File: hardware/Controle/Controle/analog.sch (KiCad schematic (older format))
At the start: 19 parts

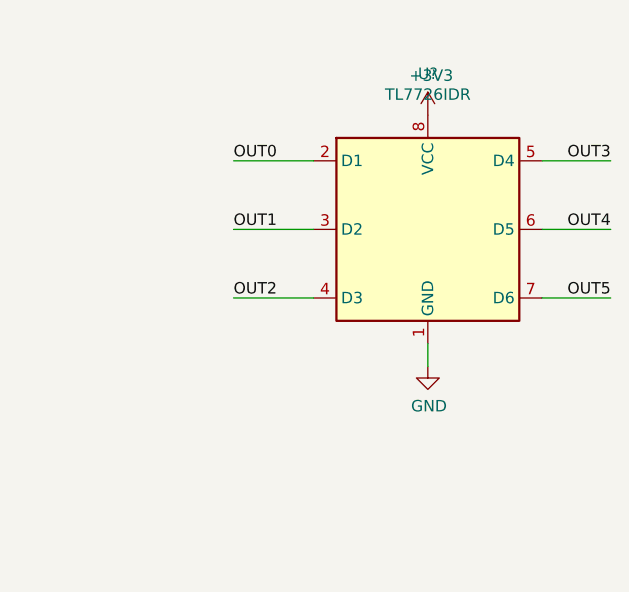
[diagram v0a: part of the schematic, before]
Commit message: adicionado o TL7726 e modificada a placa
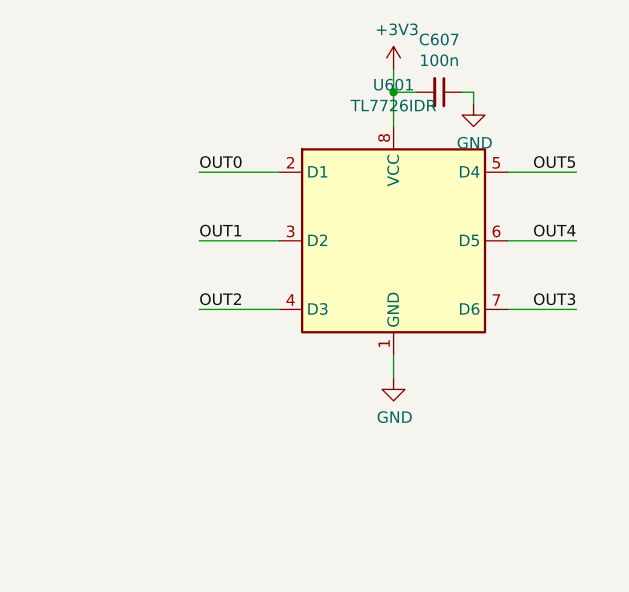
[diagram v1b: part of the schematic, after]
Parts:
- added C607: 100n, Capacitor_SMD:C_0603_1608Metric_Pad1.08x0.95mm_HandSolder, symbol Device:C_Small
- U601: renamed from U?; footprint Package_SON:X2SON-8_1.4x1mm_P0.35mm -> Package_SO:SOIC-8_3.9x4.9mm_P1.27mm
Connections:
- net +3V3: now also C607.2
- net GND: now also C607.1
- net Out3: now also U601.7 (D6); no longer U601.5 (D4)
- net Out5: now also U601.5 (D4); no longer U601.7 (D6)
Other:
- moved on the sheet: U601
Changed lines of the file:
@@
 In0
 $Comp
-L tl7726:TL7726IDR U?
+L tl7726:TL7726IDR U601
 U 1 1 60A10993
-P 5000 1400
-F 0 "U?" H 5000 2081 50  0000 C CNN
-F 1 "TL7726IDR" H 5000 1990 50  0000 C CNN
-F 2 "Package_SON:X2SON-8_1.4x1mm_P0.35mm" H 4050 900 50  0001 C CNN
-F 3 "http://www.ti.com/lit/ds/symlink/tpd4s1394.pdf" H 4900 1350 50  0001 C CNN
-	1    5000 1400
+P 4850 1450
+F 0 "U601" H 4850 2131 50  0000 C CNN
+F 1 "TL7726IDR" H 4850 2040 50  0000 C CNN
+F 2 "Package_SO:SOIC-8_3.9x4.9mm_P1.27mm" H 3900 950 50  0001 C CNN
+F 3 "http://www.ti.com/lit/ds/symlink/tpd4s1394.pdf" H 4750 1400 50  0001 C CNN
+	1    4850 1450
 	1    0    0    -1
 $EndComp
@@
 Text Label 2350 4350 0    50   ~ 0
 OUT5
-Text Label 4150 1100 0    50   ~ 0
+Text Label 4000 1150 0    50   ~ 0
 OUT0
 Wire Wire Line
-	4150 1100 4500 1100
-Text Label 4150 1400 0    50   ~ 0
+	4000 1150 4350 1150
+Text Label 4000 1450 0    50   ~ 0
 OUT1
 Wire Wire Line
-	4150 1400 4500 1400
-Text Label 4150 1700 0    50   ~ 0
+	4000 1450 4350 1450
+Text Label 4000 1750 0    50   ~ 0
 OUT2
 Wire Wire Line
-	4150 1700 4500 1700
-Text Label 5800 1100 2    50   ~ 0
+	4000 1750 4350 1750
+Text Label 5650 1750 2    50   ~ 0
 OUT3
 Wire Wire Line
-	5800 1100 5500 1100
-Text Label 5800 1400 2    50   ~ 0
+	5650 1150 5350 1150
+Text Label 5650 1450 2    50   ~ 0
 OUT4
 Wire Wire Line
-	5800 1400 5500 1400
-Text Label 5800 1700 2    50   ~ 0
+	5650 1450 5350 1450
+Text Label 5650 1150 2    50   ~ 0
 OUT5
 Wire Wire Line
-	5800 1700 5500 1700
+	5650 1750 5350 1750
 $Comp
-L power:GND #PWR?
+L power:GND #PWR0119
 U 1 1 60A2814F
-P 5000 2000
-F 0 "#PWR?" H 5000 1750 50  0001 C CNN
-F 1 "GND" H 5005 1827 50  0000 C CNN
-F 2 "" H 5000 2000 50  0001 C CNN
-F 3 "" H 5000 2000 50  0001 C CNN
-	1    5000 2000
+P 4850 2050
+F 0 "#PWR0119" H 4850 1800 50  0001 C CNN
+F 1 "GND" H 4855 1877 50  0000 C CNN
+F 2 "" H 4850 2050 50  0001 C CNN
+F 3 "" H 4850 2050 50  0001 C CNN
+	1    4850 2050
 	1    0    0    -1
 $EndComp
 Wire Wire Line
-	5000 2000 5000 1900
+	4850 2050 4850 1950
 $Comp
-L power:+3V3 #PWR?
+L power:+3V3 #PWR0120
 U 1 1 60A2A838
 P 1000 2350
-F 0 "#PWR?" H 1000 2200 50  0001 C CNN
+F 0 "#PWR0120" H 1000 2200 50  0001 C CNN
 F 1 "+3V3" H 1015 2523 50  0000 C CNN
 F 2 "" H 1000 2350 50  0001 C CNN
@@
 	1000 2550 1000 2350
 $Comp
-L power:+3V3 #PWR?
+L power:+3V3 #PWR0121
 U 1 1 60A2DB9D
-P 5000 900
-F 0 "#PWR?" H 5000 750 50  0001 C CNN
-F 1 "+3V3" H 5015 1073 50  0000 C CNN
-F 2 "" H 5000 900 50  0001 C CNN
-F 3 "" H 5000 900 50  0001 C CNN
-	1    5000 900
+P 4850 700
+F 0 "#PWR0121" H 4850 550 50  0001 C CNN
+F 1 "+3V3" H 4865 873 50  0000 C CNN
+F 2 "" H 4850 700 50  0001 C CNN
+F 3 "" H 4850 700 50  0001 C CNN
+	1    4850 700
 	1    0    0    -1
 $EndComp
@@
 Wire Wire Line
 	2100 4350 2600 4350
+$Comp
+L Device:C_Small C607
+U 1 1 60A6394D
+P 5050 800
+F 0 "C607" V 4821 800 50  0000 C CNN
+F 1 "100n" V 4912 800 50  0000 C CNN
+F 2 "Capacitor_SMD:C_0603_1608Metric_Pad1.08x0.95mm_HandSolder" H 5050 800 50  0001 C CNN
+F 3 "~" H 5050 800 50  0001 C CNN
+	1    5050 800
+	0    1    1    0
+$EndComp
+Wire Wire Line
+	4850 700  4850 800
+$Comp
+L power:GND #PWR0122
+U 1 1 60A69EE4
+P 5200 850
+F 0 "#PWR0122" H 5200 600 50  0001 C CNN
+F 1 "GND" H 5205 677 50  0000 C CNN
+F 2 "" H 5200 850 50  0001 C CNN
+F 3 "" H 5200 850 50  0001 C CNN
+	1    5200 850
+	1    0    0    -1
+$EndComp
+Wire Wire Line
+	5200 850  5200 800
+Wire Wire Line
+	5200 800  5150 800
+Wire Wire Line
+	4950 800  4850 800
+Connection ~ 4850 800
+Wire Wire Line
+	4850 800  4850 950
 $EndSCHEMATC

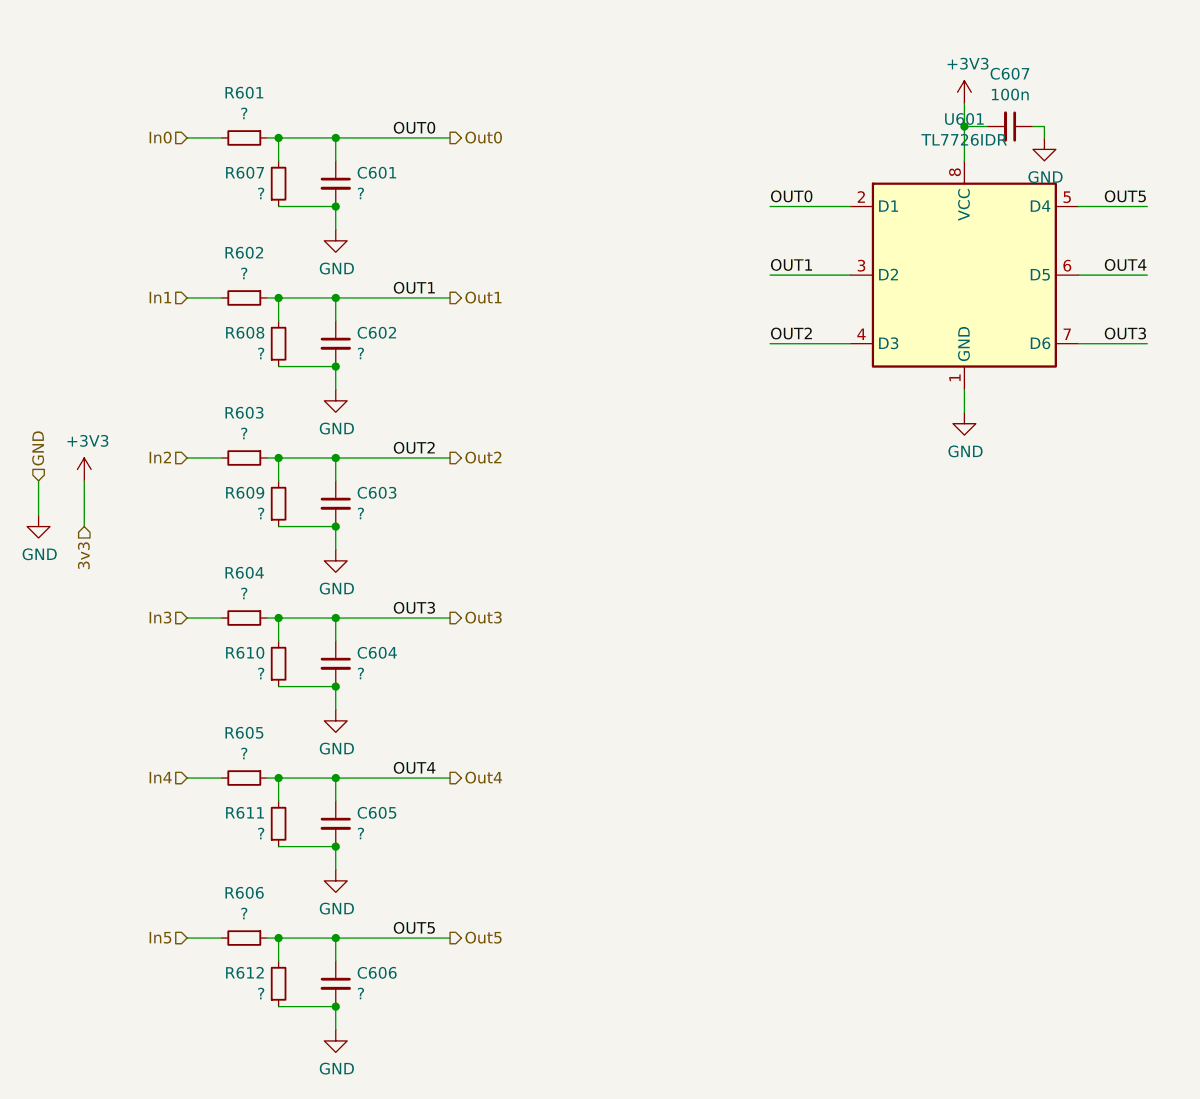
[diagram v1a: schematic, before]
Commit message: control PCB updated
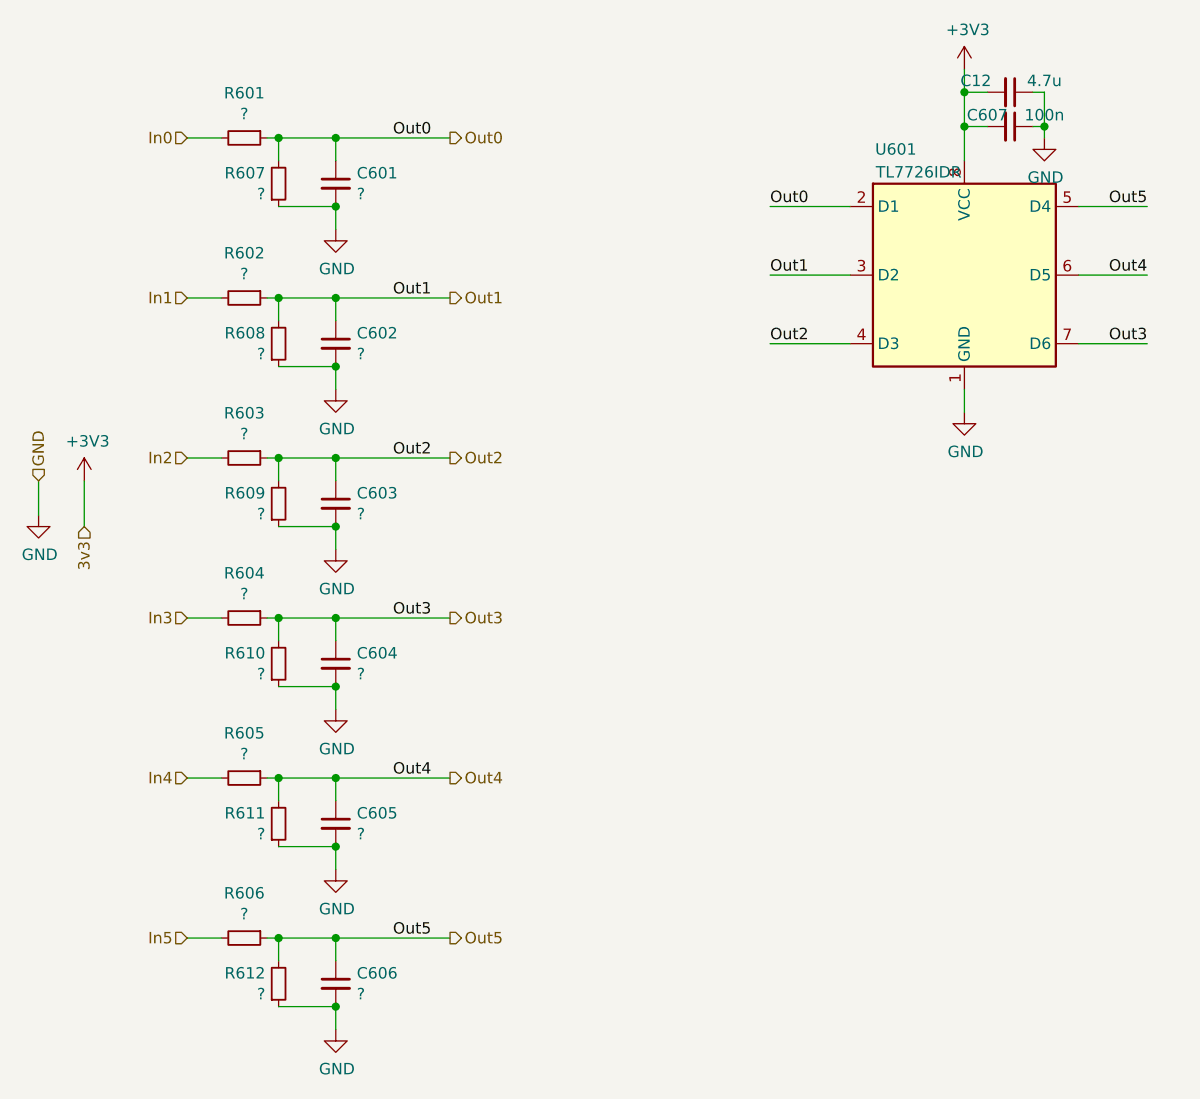
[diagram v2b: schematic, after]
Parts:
- added C12: 4.7u, Capacitor_SMD:C_1210_3225Metric_Pad1.33x2.70mm_HandSolder, symbol Device:C_Small
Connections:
- net +3V3: now also C12.2
- net GND: now also C12.1
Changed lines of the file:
@@
 U 1 1 60A10993
 P 4850 1450
-F 0 "U601" H 4850 2131 50  0000 C CNN
-F 1 "TL7726IDR" H 4850 2040 50  0000 C CNN
+F 0 "U601" H 4550 2000 50  0000 C CNN
+F 1 "TL7726IDR" H 4650 1900 50  0000 C CNN
 F 2 "Package_SO:SOIC-8_3.9x4.9mm_P1.27mm" H 3900 950 50  0001 C CNN
 F 3 "http://www.ti.com/lit/ds/symlink/tpd4s1394.pdf" H 4750 1400 50  0001 C CNN
@@
 $EndComp
 Text Label 2350 850  0    50   ~ 0
-OUT0
+Out0
 Text Label 2350 1550 0    50   ~ 0
-OUT1
+Out1
 Text Label 2350 2250 0    50   ~ 0
-OUT2
+Out2
 Text Label 2350 2950 0    50   ~ 0
-OUT3
+Out3
 Text Label 2350 3650 0    50   ~ 0
-OUT4
+Out4
 Text Label 2350 4350 0    50   ~ 0
-OUT5
+Out5
 Text Label 4000 1150 0    50   ~ 0
-OUT0
+Out0
 Wire Wire Line
 	4000 1150 4350 1150
 Text Label 4000 1450 0    50   ~ 0
-OUT1
+Out1
 Wire Wire Line
 	4000 1450 4350 1450
 Text Label 4000 1750 0    50   ~ 0
-OUT2
+Out2
 Wire Wire Line
 	4000 1750 4350 1750
 Text Label 5650 1750 2    50   ~ 0
-OUT3
+Out3
 Wire Wire Line
 	5650 1150 5350 1150
 Text Label 5650 1450 2    50   ~ 0
-OUT4
+Out4
 Wire Wire Line
 	5650 1450 5350 1450
 Text Label 5650 1150 2    50   ~ 0
-OUT5
+Out5
 Wire Wire Line
 	5650 1750 5350 1750
@@
 L power:+3V3 #PWR0121
 U 1 1 60A2DB9D
-P 4850 700
-F 0 "#PWR0121" H 4850 550 50  0001 C CNN
-F 1 "+3V3" H 4865 873 50  0000 C CNN
-F 2 "" H 4850 700 50  0001 C CNN
-F 3 "" H 4850 700 50  0001 C CNN
-	1    4850 700
+P 4850 550
+F 0 "#PWR0121" H 4850 400 50  0001 C CNN
+F 1 "+3V3" H 4865 723 50  0000 C CNN
+F 2 "" H 4850 550 50  0001 C CNN
+F 3 "" H 4850 550 50  0001 C CNN
+	1    4850 550
 	1    0    0    -1
 $EndComp
@@
 U 1 1 60A6394D
 P 5050 800
-F 0 "C607" V 4821 800 50  0000 C CNN
-F 1 "100n" V 4912 800 50  0000 C CNN
+F 0 "C607" V 5000 700 50  0000 C CNN
+F 1 "100n" V 5000 950 50  0000 C CNN
 F 2 "Capacitor_SMD:C_0603_1608Metric_Pad1.08x0.95mm_HandSolder" H 5050 800 50  0001 C CNN
 F 3 "~" H 5050 800 50  0001 C CNN
@@
 $EndComp
 Wire Wire Line
-	4850 700  4850 800
+	4850 550  4850 650
 $Comp
 L power:GND #PWR0122
@@
 Wire Wire Line
 	4850 800  4850 950
+$Comp
+L Device:C_Small C12
+U 1 1 607A1571
+P 5050 650
+F 0 "C12" V 5000 500 50  0000 C CNN
+F 1 "4.7u" V 5000 800 50  0000 C CNN
+F 2 "Capacitor_SMD:C_1210_3225Metric_Pad1.33x2.70mm_HandSolder" H 5050 650 50  0001 C CNN
+F 3 "~" H 5050 650 50  0001 C CNN
+	1    5050 650
+	0    1    1    0
+$EndComp
+Wire Wire Line
+	5150 650  5200 650
+Wire Wire Line
+	5200 650  5200 800
+Connection ~ 5200 800
+Wire Wire Line
+	4950 650  4850 650
+Connection ~ 4850 650
+Wire Wire Line
+	4850 650  4850 800
 $EndSCHEMATC

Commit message: falta acabamento
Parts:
- C12: footprint Capacitor_SMD:C_1210_3225Metric_Pad1.33x2.70mm_HandSolder -> Capacitor_SMD:C_1206_3216Metric_Pad1.33x1.80mm_HandSolder
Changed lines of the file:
@@
 F 0 "C12" V 5000 500 50  0000 C CNN
 F 1 "4.7u" V 5000 800 50  0000 C CNN
-F 2 "Capacitor_SMD:C_1210_3225Metric_Pad1.33x2.70mm_HandSolder" H 5050 650 50  0001 C CNN
+F 2 "Capacitor_SMD:C_1206_3216Metric_Pad1.33x1.80mm_HandSolder" H 5050 650 50  0001 C CNN
 F 3 "~" H 5050 650 50  0001 C CNN
 	1    5050 650

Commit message: vias
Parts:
- C601, C602, C603: value ? -> 1n
- C604: value ? -> 100n
- R601, R602, R603: value ? -> 10k
- R604: value ? -> 0R
- R605, R606, R610, R611, R612: value ? -> NC
- R607, R608, R609: value ? -> 3k3
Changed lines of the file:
@@
 P 1700 1550
 F 0 "R602" V 1504 1550 50  0000 C CNN
-F 1 "?" V 1595 1550 50  0000 C CNN
+F 1 "10k" V 1595 1550 50  0000 C CNN
 F 2 "Resistor_SMD:R_0603_1608Metric_Pad0.98x0.95mm_HandSolder" H 1700 1550 50  0001 C CNN
 F 3 "~" H 1700 1550 50  0001 C CNN
@@
 P 2100 1750
 F 0 "C602" H 2192 1796 50  0000 L CNN
-F 1 "?" H 2192 1705 50  0000 L CNN
+F 1 "1n" H 2192 1705 50  0000 L CNN
 F 2 "Capacitor_SMD:C_0603_1608Metric_Pad1.08x0.95mm_HandSolder" H 2100 1750 50  0001 C CNN
 F 3 "~" H 2100 1750 50  0001 C CNN
@@
 P 1850 1750
 F 0 "R608" H 1792 1704 50  0000 R CNN
-F 1 "?" H 1792 1795 50  0000 R CNN
+F 1 "3k3" H 1792 1795 50  0000 R CNN
 F 2 "Resistor_SMD:R_0603_1608Metric_Pad0.98x0.95mm_HandSolder" H 1850 1750 50  0001 C CNN
 F 3 "~" H 1850 1750 50  0001 C CNN
@@
 P 1700 2250
 F 0 "R603" V 1504 2250 50  0000 C CNN
-F 1 "?" V 1595 2250 50  0000 C CNN
+F 1 "10k" V 1595 2250 50  0000 C CNN
 F 2 "Resistor_SMD:R_0603_1608Metric_Pad0.98x0.95mm_HandSolder" H 1700 2250 50  0001 C CNN
 F 3 "~" H 1700 2250 50  0001 C CNN
@@
 P 2100 2450
 F 0 "C603" H 2192 2496 50  0000 L CNN
-F 1 "?" H 2192 2405 50  0000 L CNN
+F 1 "1n" H 2192 2405 50  0000 L CNN
 F 2 "Capacitor_SMD:C_0603_1608Metric_Pad1.08x0.95mm_HandSolder" H 2100 2450 50  0001 C CNN
 F 3 "~" H 2100 2450 50  0001 C CNN
@@
 P 1850 2450
 F 0 "R609" H 1792 2404 50  0000 R CNN
-F 1 "?" H 1792 2495 50  0000 R CNN
+F 1 "3k3" H 1792 2495 50  0000 R CNN
 F 2 "Resistor_SMD:R_0603_1608Metric_Pad0.98x0.95mm_HandSolder" H 1850 2450 50  0001 C CNN
 F 3 "~" H 1850 2450 50  0001 C CNN
@@
 P 1700 2950
 F 0 "R604" V 1504 2950 50  0000 C CNN
-F 1 "?" V 1595 2950 50  0000 C CNN
+F 1 "0R" V 1595 2950 50  0000 C CNN
 F 2 "Resistor_SMD:R_0603_1608Metric_Pad0.98x0.95mm_HandSolder" H 1700 2950 50  0001 C CNN
 F 3 "~" H 1700 2950 50  0001 C CNN
@@
 P 2100 3150
 F 0 "C604" H 2192 3196 50  0000 L CNN
-F 1 "?" H 2192 3105 50  0000 L CNN
+F 1 "100n" H 2192 3105 50  0000 L CNN
 F 2 "Capacitor_SMD:C_0603_1608Metric_Pad1.08x0.95mm_HandSolder" H 2100 3150 50  0001 C CNN
 F 3 "~" H 2100 3150 50  0001 C CNN
@@
 P 1850 3150
 F 0 "R610" H 1792 3104 50  0000 R CNN
-F 1 "?" H 1792 3195 50  0000 R CNN
+F 1 "NC" H 1792 3195 50  0000 R CNN
 F 2 "Resistor_SMD:R_0603_1608Metric_Pad0.98x0.95mm_HandSolder" H 1850 3150 50  0001 C CNN
 F 3 "~" H 1850 3150 50  0001 C CNN
@@
 P 1700 3650
 F 0 "R605" V 1504 3650 50  0000 C CNN
-F 1 "?" V 1595 3650 50  0000 C CNN
+F 1 "NC" V 1595 3650 50  0000 C CNN
 F 2 "Resistor_SMD:R_0603_1608Metric_Pad0.98x0.95mm_HandSolder" H 1700 3650 50  0001 C CNN
 F 3 "~" H 1700 3650 50  0001 C CNN
@@
 P 1850 3850
 F 0 "R611" H 1792 3804 50  0000 R CNN
-F 1 "?" H 1792 3895 50  0000 R CNN
+F 1 "NC" H 1792 3895 50  0000 R CNN
 F 2 "Resistor_SMD:R_0603_1608Metric_Pad0.98x0.95mm_HandSolder" H 1850 3850 50  0001 C CNN
 F 3 "~" H 1850 3850 50  0001 C CNN
@@
 P 1700 4350
 F 0 "R606" V 1504 4350 50  0000 C CNN
-F 1 "?" V 1595 4350 50  0000 C CNN
+F 1 "NC" V 1595 4350 50  0000 C CNN
 F 2 "Resistor_SMD:R_0603_1608Metric_Pad0.98x0.95mm_HandSolder" H 1700 4350 50  0001 C CNN
 F 3 "~" H 1700 4350 50  0001 C CNN
@@
 P 1850 4550
 F 0 "R612" H 1792 4504 50  0000 R CNN
-F 1 "?" H 1792 4595 50  0000 R CNN
+F 1 "NC" H 1792 4595 50  0000 R CNN
 F 2 "Resistor_SMD:R_0603_1608Metric_Pad0.98x0.95mm_HandSolder" H 1850 4550 50  0001 C CNN
 F 3 "~" H 1850 4550 50  0001 C CNN
@@
 P 1850 1050
 F 0 "R607" H 1792 1004 50  0000 R CNN
-F 1 "?" H 1792 1095 50  0000 R CNN
+F 1 "3k3" H 1792 1095 50  0000 R CNN
 F 2 "Resistor_SMD:R_0603_1608Metric_Pad0.98x0.95mm_HandSolder" H 1850 1050 50  0001 C CNN
 F 3 "~" H 1850 1050 50  0001 C CNN
@@
 P 2100 1050
 F 0 "C601" H 2192 1096 50  0000 L CNN
-F 1 "?" H 2192 1005 50  0000 L CNN
+F 1 "1n" H 2192 1005 50  0000 L CNN
 F 2 "Capacitor_SMD:C_0603_1608Metric_Pad1.08x0.95mm_HandSolder" H 2100 1050 50  0001 C CNN
 F 3 "~" H 2100 1050 50  0001 C CNN
@@
 P 1700 850
 F 0 "R601" V 1504 850 50  0000 C CNN
-F 1 "?" V 1595 850 50  0000 C CNN
+F 1 "10k" V 1595 850 50  0000 C CNN
 F 2 "Resistor_SMD:R_0603_1608Metric_Pad0.98x0.95mm_HandSolder" H 1700 850 50  0001 C CNN
 F 3 "~" H 1700 850 50  0001 C CNN

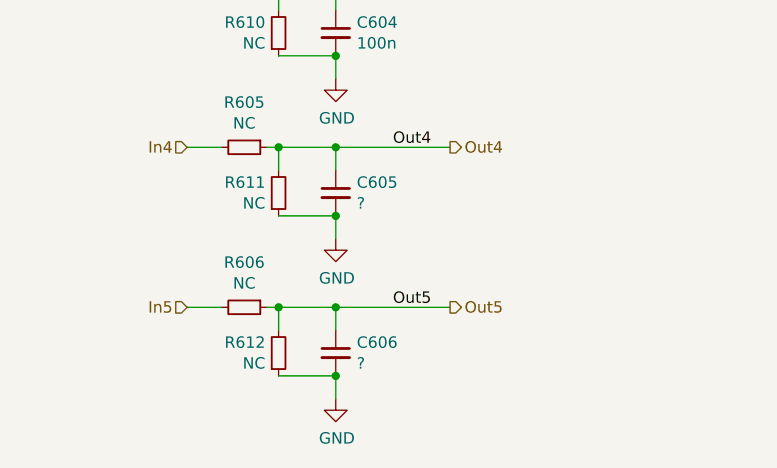
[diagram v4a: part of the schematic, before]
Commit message: dimensions and holes modified
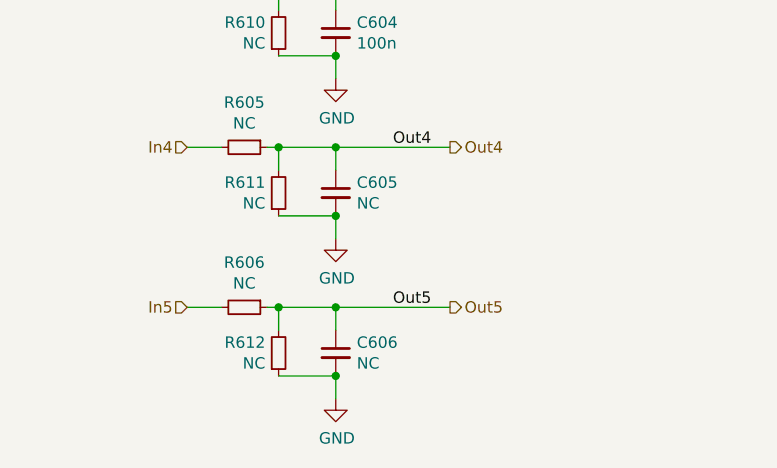
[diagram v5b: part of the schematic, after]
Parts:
- C605, C606: value ? -> NC
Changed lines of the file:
@@
 P 2100 3850
 F 0 "C605" H 2192 3896 50  0000 L CNN
-F 1 "?" H 2192 3805 50  0000 L CNN
+F 1 "NC" H 2192 3805 50  0000 L CNN
 F 2 "Capacitor_SMD:C_0603_1608Metric_Pad1.08x0.95mm_HandSolder" H 2100 3850 50  0001 C CNN
 F 3 "~" H 2100 3850 50  0001 C CNN
@@
 P 2100 4550
 F 0 "C606" H 2192 4596 50  0000 L CNN
-F 1 "?" H 2192 4505 50  0000 L CNN
+F 1 "NC" H 2192 4505 50  0000 L CNN
 F 2 "Capacitor_SMD:C_0603_1608Metric_Pad1.08x0.95mm_HandSolder" H 2100 4550 50  0001 C CNN
 F 3 "~" H 2100 4550 50  0001 C CNN
